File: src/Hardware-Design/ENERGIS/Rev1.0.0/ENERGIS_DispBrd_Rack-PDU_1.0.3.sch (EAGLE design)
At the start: 75 parts, among them CON1 DNI, CON2 AFC11-S20ICC-00, IC1 MCP23017T-E/ML, IC2 MCP23017T-E/ML, T1 BSS138

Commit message: update documentation
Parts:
- removed D1, D2, D3, D4: PTVS3V3S1UR,115, ds_diode:PTVS3V3S1UR,115
- removed D5: RCLAMP0582BQTCT, ds_diode:RCLAMP0582BQTCT
- removed R16, R17, R18, R19: 10K 1%, ds_resistor:10K-1%0402
- R12, R13, R5, R6: value 33K 1% -> 10K 1%; device ds_resistor:33K-1%0402 -> ds_resistor:10K-1%0402
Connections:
- removed net N$24: D3.C, O.P$2, R18.1
- removed net N$25: D4.C, PWR.P$2, R19.1
- removed net N$26: >.P$2, D1.C, R17.1
- removed net N$7: <.P$2, D2.C, R16.1
- net GND: no longer D1.A, D2.A, D3.A, D4.A, D5.3
- net I2C0_SCL: no longer D5.1
- net I2C0_SDA: no longer D5.2
- net KEY_0: now also <.P$2; no longer R16.2
- net KEY_1: now also >.P$2; no longer R17.2
- net KEY_2: now also O.P$2; no longer R18.2
- net KEY_3: now also PWR.P$2; no longer R19.2
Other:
- moved on the sheet: <, >, C10, C11, C12, C5, C6, C7, C8, C9, CH1, CH2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

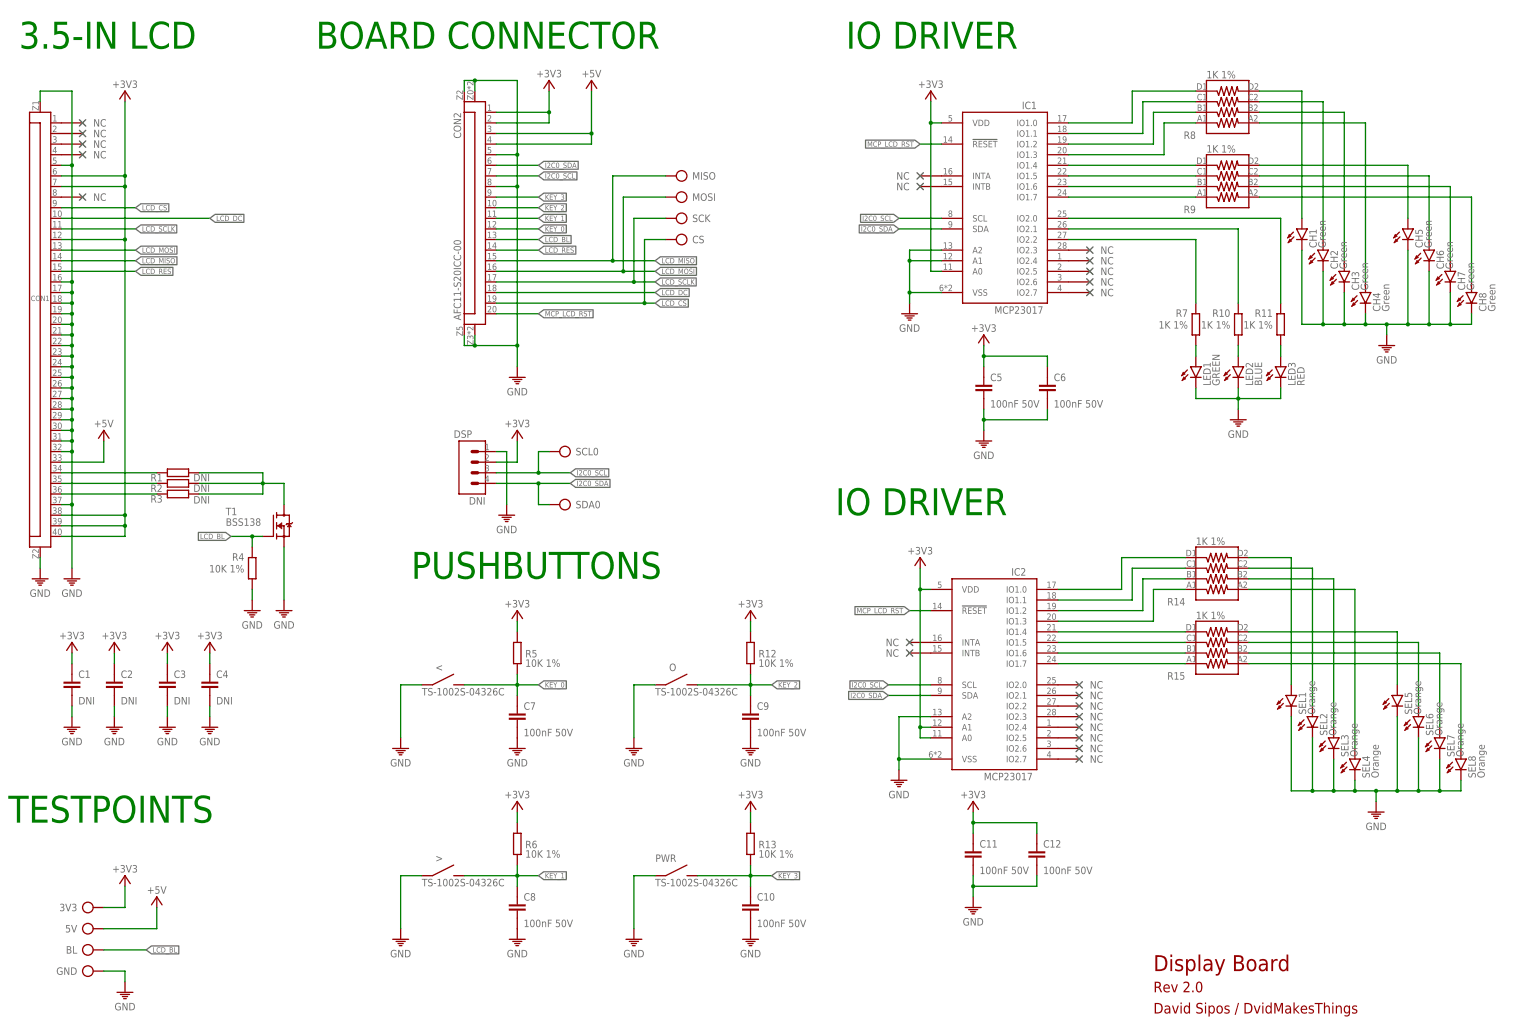
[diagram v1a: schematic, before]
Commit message: Add software ESD protection to button control and port expanders. Design sheet metal shielding around electronics. Add ethernet test
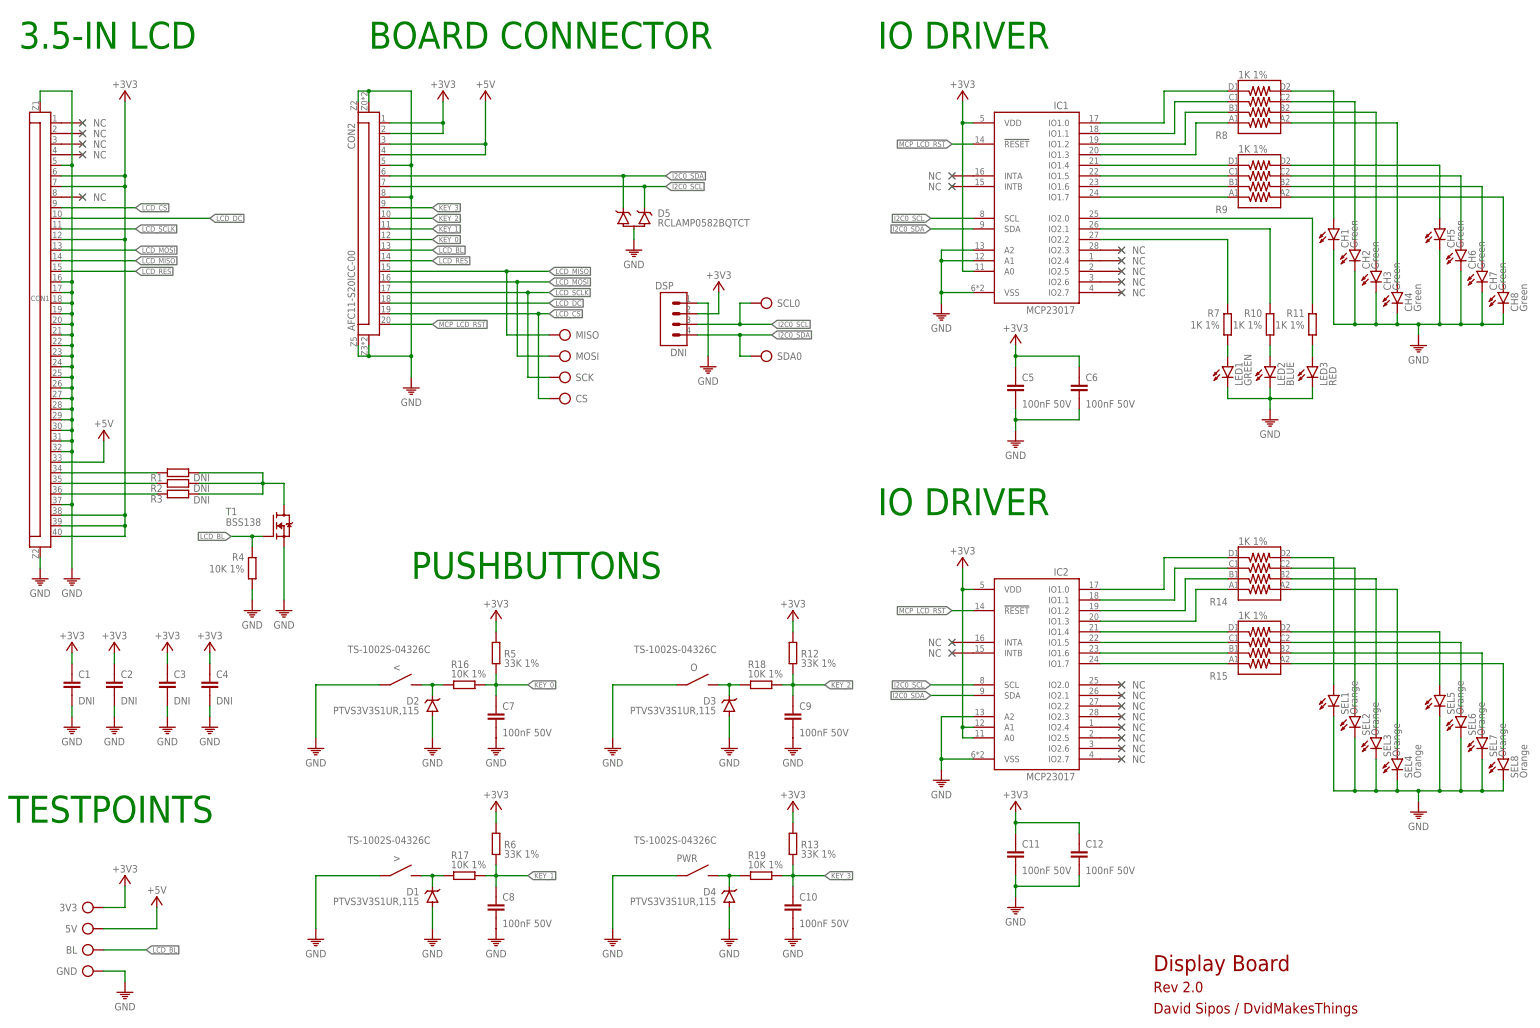
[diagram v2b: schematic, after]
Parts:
- added D1, D2, D3, D4: PTVS3V3S1UR,115, ds_diode:PTVS3V3S1UR,115
- added D5: RCLAMP0582BQTCT, ds_diode:RCLAMP0582BQTCT
- added R16, R17, R18, R19: 10K 1%, ds_resistor:10K-1%0402
- R12, R13, R5, R6: value 10K 1% -> 33K 1%; device ds_resistor:10K-1%0402 -> ds_resistor:33K-1%0402
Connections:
- new net N$24: D3.C, O.P$2, R18.1
- new net N$25: D4.C, PWR.P$2, R19.1
- new net N$26: >.P$2, D1.C, R17.1
- new net N$7: <.P$2, D2.C, R16.1
- net GND: now also D1.A, D2.A, D3.A, D4.A, D5.3
- net I2C0_SCL: now also D5.1
- net I2C0_SDA: now also D5.2
- net KEY_0: now also R16.2; no longer <.P$2
- net KEY_1: now also R17.2; no longer >.P$2
- net KEY_2: now also R18.2; no longer O.P$2
- net KEY_3: now also R19.2; no longer PWR.P$2
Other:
- moved on the sheet: <, >, C10, C11, C12, C5, C6, C7, C8, C9, CH1, CH2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
